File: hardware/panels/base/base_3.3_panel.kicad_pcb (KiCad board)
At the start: 2 copper layers, 77 x 93 mm, 50 parts, among them IC1 single_pad_smd, IC2 single_pad_smd, J1 Conn 1, J2 Conn 2

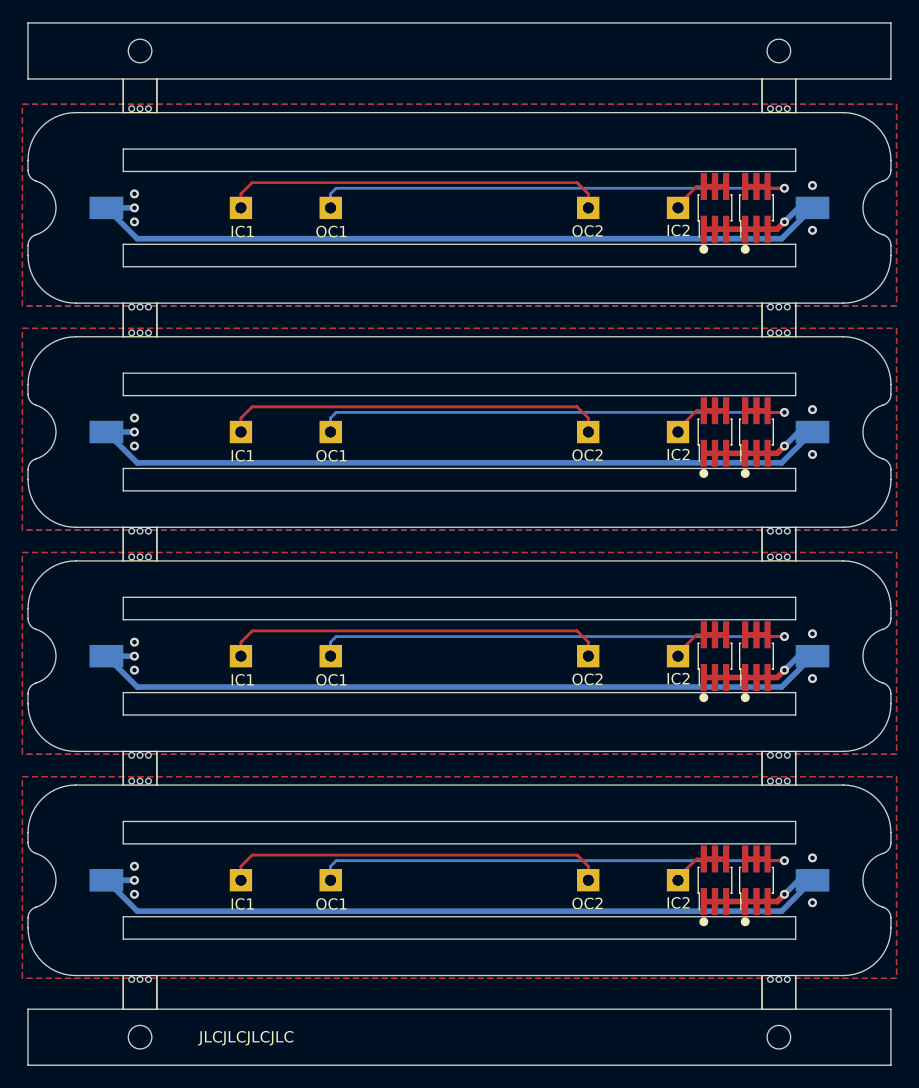
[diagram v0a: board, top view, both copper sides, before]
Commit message: Base PCB panels updates
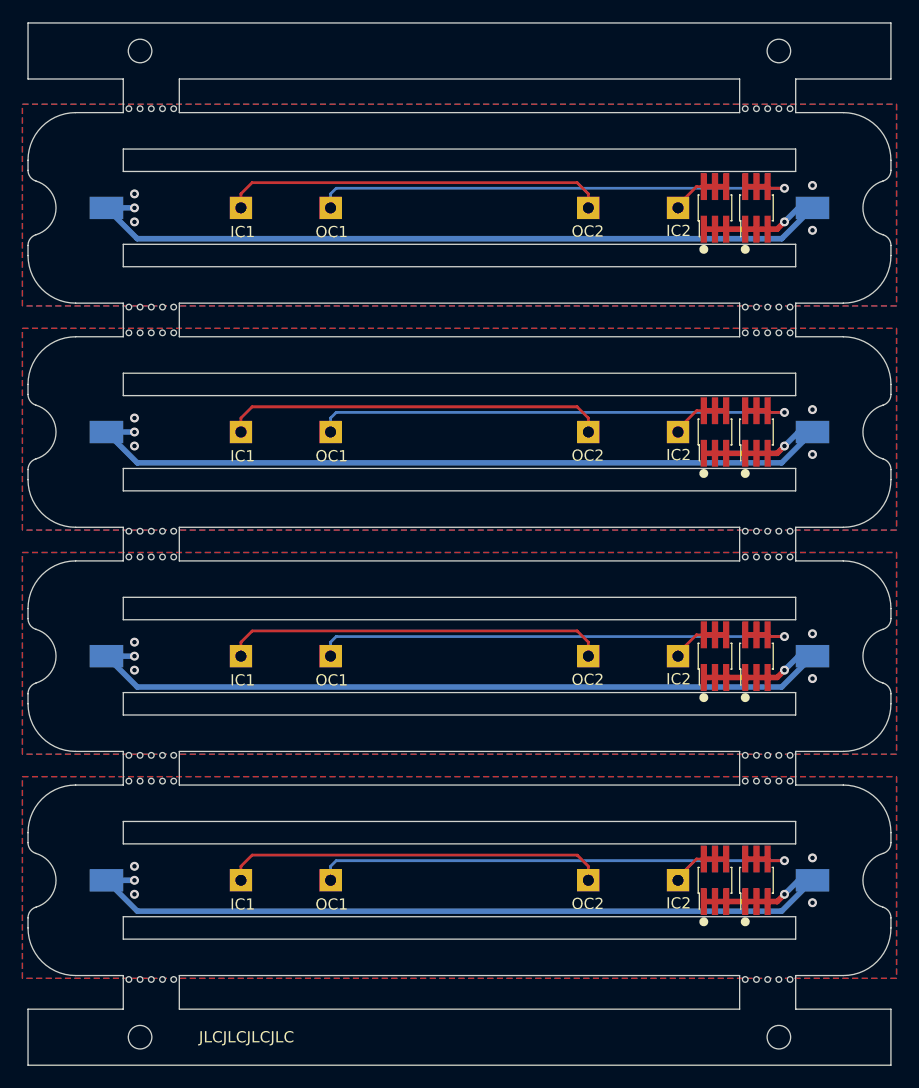
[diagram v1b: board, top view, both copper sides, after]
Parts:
- moved mouse-bite-3mm-slot 1.00 mm to (110.0, 117.5)
- moved mouse-bite-3mm-slot 1.00 mm to (55.0, 57.5)
- moved mouse-bite-3mm-slot 1.00 mm to (55.0, 117.5)
- moved mouse-bite-3mm-slot 1.00 mm to (110.0, 37.5)
- moved mouse-bite-3mm-slot 1.00 mm to (55.0, 37.5)
- moved mouse-bite-3mm-slot 1.00 mm to (110.0, 97.5)
- moved mouse-bite-3mm-slot 1.00 mm to (110.0, 77.5)
- moved mouse-bite-3mm-slot 1.00 mm to (110.0, 57.5)
- moved mouse-bite-3mm-slot 1.00 mm to (55.0, 97.5)
- moved mouse-bite-3mm-slot 1.00 mm to (55.0, 77.5)
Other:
- outline, holes or cut-outs redrawn
